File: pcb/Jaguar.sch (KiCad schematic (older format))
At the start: 49 parts, among them P1 12v-SW, P10 TPS, P11 Sensor-GND, P12 O2, P13 Sensor-GND, P14 RPM0+, P15 RPM0-, P16 RPM1+, P17 RPM1-, P20 PT4-7, P22 INJ1-GND, P25 FUEL-, P3 GND, P31 OUT-GND, P32 OUTPUT-12v, P33 Injectors-PB, P34 Injectors-IN, P35 FAN-, P37 ACC-, P39 FAN, P4 BRV-12v, P40 ACC, P41 MAF, P42 INJ2-GND, P43 RPM0-Shield, P44 RPM1-Shield, P45 Sensor-GND, P5 GND2, P50 INJ3-GND, P51 INJ4-GND, P52 INJ8-GND, P53 INJ7-GND, P54 INJ6-GND, P55 INJ5-GND, P56 MAF-CPU-Signal, P6 IAT, P61 Fan-Out, P62 PK5, P7 MAT, P72 INJ1, P73 INJ2, P74 INJ3, P75 INJ4, P76 INJ5, P77 INJ6, P78 INJ7, P79 INJ8, P8 CHT, P9 TPS-5v

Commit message: Rename PK5 to PortK5, Rename FAN-OUT to PortK4, Rename ACC to LSD-2, rename ACC- to LSD2-, Rename FAN to LSD-1, rename FAN- to LSD1-, Rename OUT-GND to OUTPUT-GND.
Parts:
- P35: value FAN- -> LSD1-
- P37: value ACC- -> LSD2-
- P39: value FAN -> LSD-1
- P40: value ACC -> LSD-2
- P61: value Fan-Out -> LSD1-Out
- P62: value PK5 -> PortK5
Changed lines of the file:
@@
-EESchema Schematic File Version 2  date Sun 12 May 2013 06:47:41 PM EDT
+EESchema Schematic File Version 2  date Mon 13 May 2013 11:53:03 AM EDT
 LIBS:opto
 LIBS:power
@@
 Sheet 1 7
 Title "Jaguar PCB for FreeEMS"
-Date "12 may 2013"
+Date "13 may 2013"
 Rev "0.6-alpha"
 Comp "git hash: xxxxxxxxxx"
@@
 P 7050 2100
 F 0 "P62" H 7130 2100 40  0000 L CNN
-F 1 "PK5" H 7050 2155 30  0001 C CNN
+F 1 "PortK5" H 7050 2155 30  0001 C CNN
 	1    7050 2100
 	1    0    0    -1
@@
 P 7500 1900
 F 0 "P61" H 7580 1900 40  0000 L CNN
-F 1 "Fan-Out" H 7500 1955 30  0001 C CNN
+F 1 "LSD1-Out" H 7500 1955 30  0001 C CNN
 	1    7500 1900
 	1    0    0    -1
@@
 P 8350 3000
 F 0 "P39" H 8430 3000 40  0000 L CNN
-F 1 "FAN" H 8350 3055 30  0001 C CNN
+F 1 "LSD-1" H 8350 3055 30  0001 C CNN
 	1    8350 3000
 	-1   0    0    1
@@
 P 8900 3000
 F 0 "P40" H 8980 3000 40  0000 L CNN
-F 1 "ACC" H 8900 3055 30  0001 C CNN
+F 1 "LSD-2" H 8900 3055 30  0001 C CNN
 	1    8900 3000
 	-1   0    0    1
@@
 P 10800 3100
 F 0 "P37" H 10880 3100 40  0000 L CNN
-F 1 "ACC-" H 10800 3155 30  0001 C CNN
+F 1 "LSD2-" H 10800 3155 30  0001 C CNN
 	1    10800 3100
 	1    0    0    -1
@@
 P 10800 3000
 F 0 "P35" H 10880 3000 40  0000 L CNN
-F 1 "FAN-" H 10800 3055 30  0001 C CNN
+F 1 "LSD1-" H 10800 3055 30  0001 C CNN
 	1    10800 3000
 	1    0    0    -1

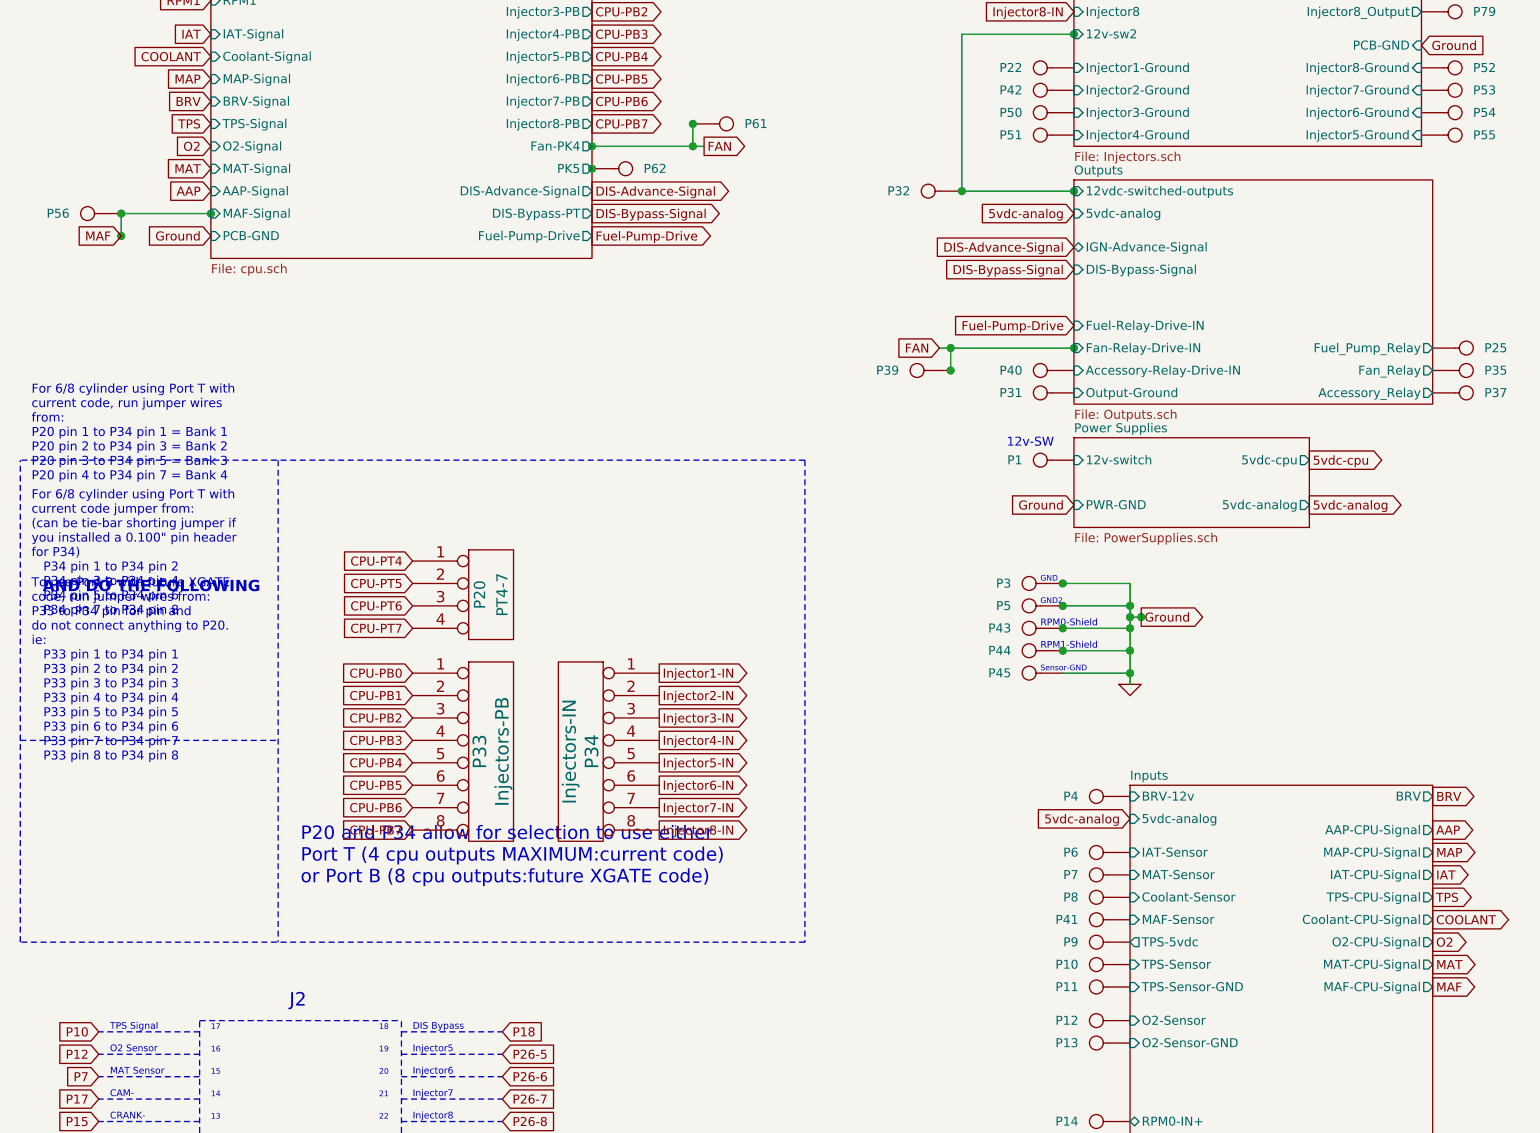
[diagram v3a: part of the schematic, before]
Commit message: Rename MAT to SPR.
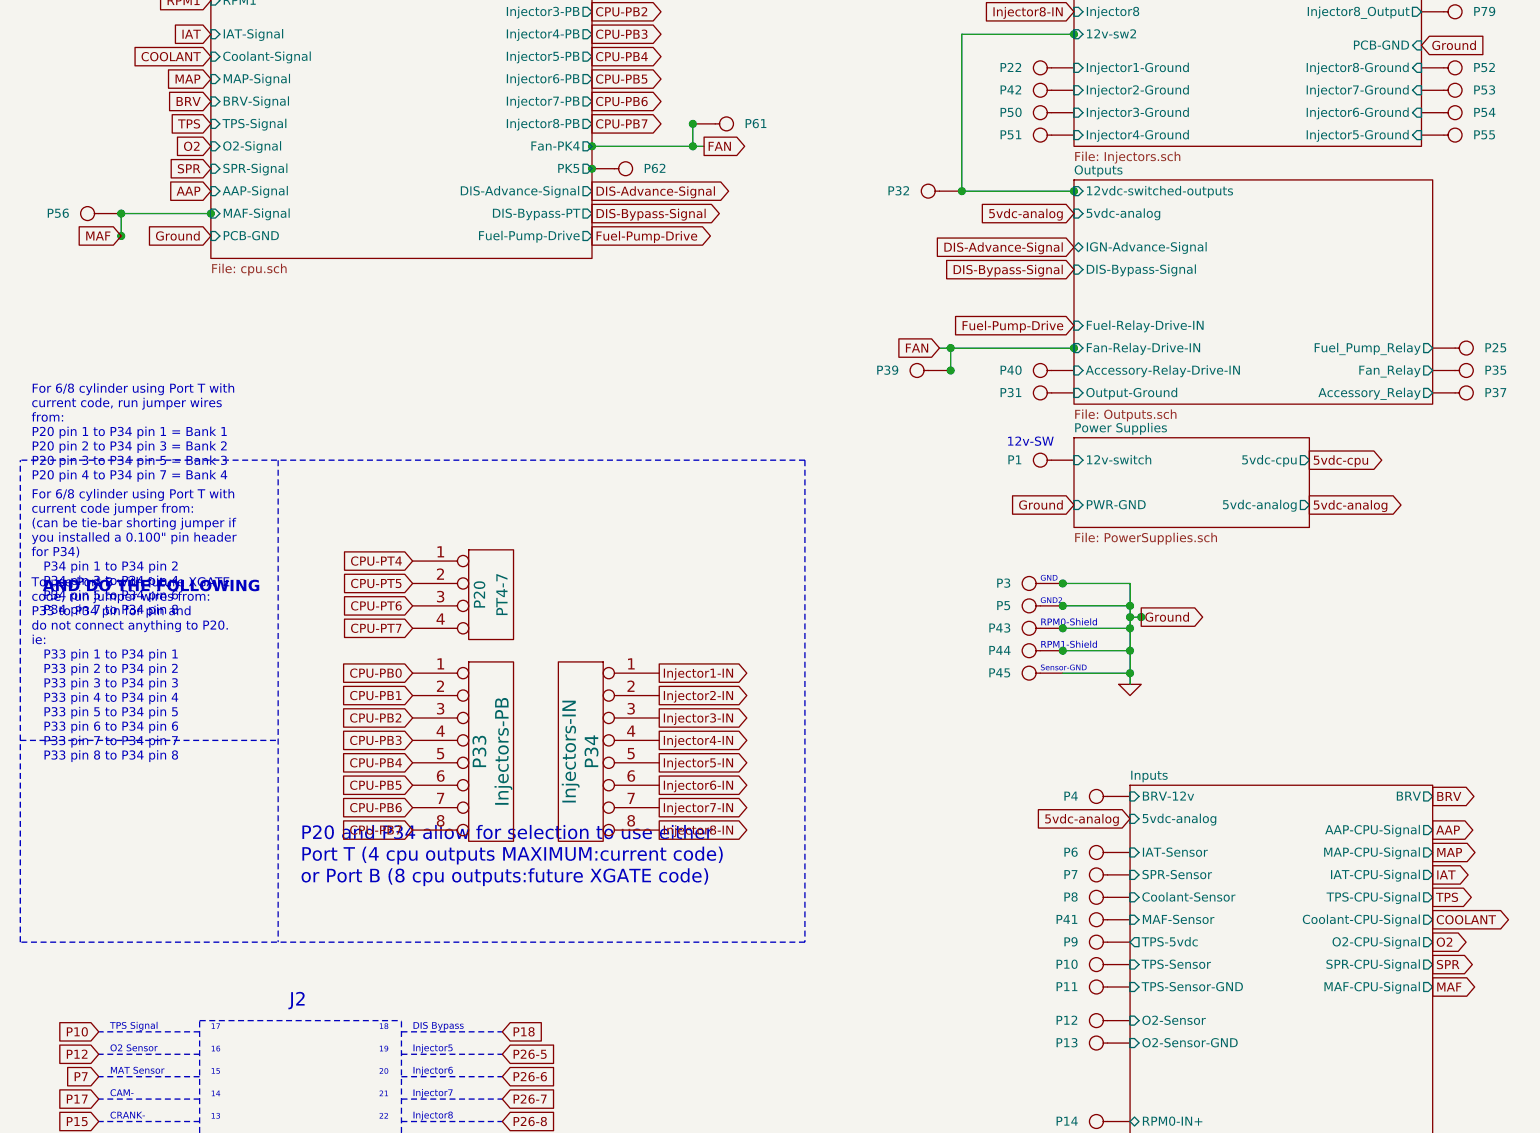
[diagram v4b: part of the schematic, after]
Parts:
- P7: value MAT -> SPR
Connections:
- net Inputs/MAT-Sensor renamed Inputs/SPR-Sensor
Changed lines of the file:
@@
-EESchema Schematic File Version 2  date Mon 13 May 2013 11:53:03 AM EDT
+EESchema Schematic File Version 2  date Mon 13 May 2013 12:23:58 PM EDT
 LIBS:opto
 LIBS:power
@@
 F3 "DIS-Advance-Signal" O R 6900 2200 40
 F4 "MAF-Signal" I L 5200 2300 40
-F5 "MAT-Signal" I L 5200 2100 40
-F6 "BRV-Signal" I L 5200 1800 40
-F7 "MAP-Signal" I L 5200 1700 40
-F8 "O2-Signal" I L 5200 2000 40
-F9 "TPS-Signal" I L 5200 1900 40
-F10 "Coolant-Signal" I L 5200 1600 40
-F11 "IAT-Signal" I L 5200 1500 40
-F12 "AAP-Signal" I L 5200 2200 40
-F13 "5vdc-analog" I L 5200 850 40
-F14 "5vdc-cpu" I L 5200 750 40
-F15 "Injector6-PB" O R 6900 1700 40
-F16 "Injector5-PB" O R 6900 1600 40
-F17 "Injector4-PB" O R 6900 1500 40
-F18 "Injector3-PB" O R 6900 1400 40
-F19 "Injector2-PB" O R 6900 1300 40
-F20 "Injector1-PB" O R 6900 1200 40
-F21 "Injector3-PT" O R 6900 950 40
-F22 "Injector2-PT" O R 6900 850 40
-F23 "Injector1-PT" O R 6900 750 40
-F24 "DIS-Bypass-PT" O R 6900 2300 40
-F25 "Injector4-PT" O R 6900 1050 40
-F26 "Injector8-PB" O R 6900 1900 40
-F27 "Injector7-PB" O R 6900 1800 40
-F28 "PCB-GND" I L 5200 2400 40
-F29 "Fan-PK4" O R 6900 2000 40
-F30 "RPM1" I L 5200 1350 40
-F31 "RPM0" I L 5200 1250 40
-F32 "PK5" O R 6900 2100 40
+F5 "BRV-Signal" I L 5200 1800 40
+F6 "MAP-Signal" I L 5200 1700 40
+F7 "O2-Signal" I L 5200 2000 40
+F8 "TPS-Signal" I L 5200 1900 40
+F9 "Coolant-Signal" I L 5200 1600 40
+F10 "IAT-Signal" I L 5200 1500 40
+F11 "AAP-Signal" I L 5200 2200 40
+F12 "5vdc-analog" I L 5200 850 40
+F13 "5vdc-cpu" I L 5200 750 40
+F14 "Injector6-PB" O R 6900 1700 40
+F15 "Injector5-PB" O R 6900 1600 40
+F16 "Injector4-PB" O R 6900 1500 40
+F17 "Injector3-PB" O R 6900 1400 40
+F18 "Injector2-PB" O R 6900 1300 40
+F19 "Injector1-PB" O R 6900 1200 40
+F20 "Injector3-PT" O R 6900 950 40
+F21 "Injector2-PT" O R 6900 850 40
+F22 "Injector1-PT" O R 6900 750 40
+F23 "DIS-Bypass-PT" O R 6900 2300 40
+F24 "Injector4-PT" O R 6900 1050 40
+F25 "Injector8-PB" O R 6900 1900 40
+F26 "Injector7-PB" O R 6900 1800 40
+F27 "PCB-GND" I L 5200 2400 40
+F28 "Fan-PK4" O R 6900 2000 40
+F29 "RPM1" I L 5200 1350 40
+F30 "RPM0" I L 5200 1250 40
+F31 "PK5" O R 6900 2100 40
+F32 "SPR-Signal" I L 5200 2100 40
 $EndSheet
 Text Notes 650  1200 0    60   ~ 0
@@
 F10 "TPS-CPU-Signal" O R 10650 5350 40
 F11 "TPS-Sensor" I L 9300 5650 40
-F12 "MAT-Sensor" I L 9300 5250 40
-F13 "MAT-CPU-Signal" O R 10650 5650 40
-F14 "BRV" O R 10650 4900 40
-F15 "MAP-CPU-Signal" O R 10650 5150 40
-F16 "BRV-12v" I L 9300 4900 40
-F17 "TPS-5vdc" O L 9300 5550 40
-F18 "5vdc-analog" I L 9300 5000 40
-F19 "MAF-Sensor" I L 9300 5450 40
-F20 "MAF-CPU-Signal" O R 10650 5750 40
-F21 "RPM1-IN-" B L 9300 6650 40
-F22 "RPM0-IN-" B L 9300 6450 40
-F23 "RPM1-IN+" B L 9300 6550 40
-F24 "RPM0-IN+" B L 9300 6350 40
-F25 "RPM1-OUT" B R 10650 6650 40
-F26 "RPM0-OUT" O R 10650 6550 40
-F27 "AAP-CPU-Signal" O R 10650 5050 40
+F12 "BRV" O R 10650 4900 40
+F13 "MAP-CPU-Signal" O R 10650 5150 40
+F14 "BRV-12v" I L 9300 4900 40
+F15 "TPS-5vdc" O L 9300 5550 40
+F16 "5vdc-analog" I L 9300 5000 40
+F17 "MAF-Sensor" I L 9300 5450 40
+F18 "MAF-CPU-Signal" O R 10650 5750 40
+F19 "RPM1-IN-" B L 9300 6650 40
+F20 "RPM0-IN-" B L 9300 6450 40
+F21 "RPM1-IN+" B L 9300 6550 40
+F22 "RPM0-IN+" B L 9300 6350 40
+F23 "RPM1-OUT" B R 10650 6650 40
+F24 "RPM0-OUT" O R 10650 6550 40
+F25 "AAP-CPU-Signal" O R 10650 5050 40
+F26 "SPR-Sensor" I L 9300 5250 40
+F27 "SPR-CPU-Signal" O R 10650 5650 40
 $EndSheet
 Text GLabel 9300 5000 0    40   Input ~ 0
@@
 P 9150 5250
 F 0 "P7" H 9230 5250 40  0000 L CNN
-F 1 "MAT" H 9150 5305 30  0001 C CNN
+F 1 "SPR" H 9150 5305 30  0001 C CNN
 	1    9150 5250
 	-1   0    0    1
@@
 COOLANT
 Text GLabel 5200 2100 0    40   Input ~ 0
-MAT
+SPR
 Text GLabel 10650 5650 2    40   Output ~ 0
-MAT
+SPR
 Text GLabel 5200 1500 0    40   Input ~ 0
 IAT

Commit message: Renamed OUTPUT-12v to IGN-12v as it wasn't clear what this pad was for.
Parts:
- P32: value OUTPUT-12v -> IGN-12v
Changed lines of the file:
@@
-EESchema Schematic File Version 2  date Mon 13 May 2013 12:23:58 PM EDT
+EESchema Schematic File Version 2  date Mon 13 May 2013 10:04:40 PM EDT
 LIBS:opto
 LIBS:power
@@
 Sheet 1 7
 Title "Jaguar PCB for FreeEMS"
-Date "13 may 2013"
+Date "14 may 2013"
 Rev "0.6-alpha"
 Comp "git hash: xxxxxxxxxx"
@@
 P 8400 2200
 F 0 "P32" H 8480 2200 40  0000 L CNN
-F 1 "OUTPUT-12v" H 8400 2255 30  0001 C CNN
+F 1 "IGN-12v" H 8400 2255 30  0001 C CNN
 	1    8400 2200
 	-1   0    0    1

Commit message: Renamed LSD2- to LSD2, renamed LSD-2 to LSD2-IN, renamed FAN- to LSD1, renamed FAN to LSD1-IN, renamed FUEL- to FUEL.
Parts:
- P25: value FUEL- -> FUEL
- P35: value LSD1- -> LSD1
- P37: value LSD2- -> LSD2
- P39: value LSD-1 -> LSD1-IN
- P40: value LSD-2 -> LSD2-IN
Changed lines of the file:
@@
-EESchema Schematic File Version 2  date Mon 13 May 2013 10:04:40 PM EDT
+EESchema Schematic File Version 2  date Tue 14 May 2013 05:29:01 PM EDT
 LIBS:opto
 LIBS:power
@@
 P 8350 3000
 F 0 "P39" H 8430 3000 40  0000 L CNN
-F 1 "LSD-1" H 8350 3055 30  0001 C CNN
+F 1 "LSD1-IN" H 8350 3055 30  0001 C CNN
 	1    8350 3000
 	-1   0    0    1
@@
 P 8900 3000
 F 0 "P40" H 8980 3000 40  0000 L CNN
-F 1 "LSD-2" H 8900 3055 30  0001 C CNN
+F 1 "LSD2-IN" H 8900 3055 30  0001 C CNN
 	1    8900 3000
 	-1   0    0    1
@@
 P 10800 3100
 F 0 "P37" H 10880 3100 40  0000 L CNN
-F 1 "LSD2-" H 10800 3155 30  0001 C CNN
+F 1 "LSD2" H 10800 3155 30  0001 C CNN
 	1    10800 3100
 	1    0    0    -1
@@
 P 10800 3000
 F 0 "P35" H 10880 3000 40  0000 L CNN
-F 1 "LSD1-" H 10800 3055 30  0001 C CNN
+F 1 "LSD1" H 10800 3055 30  0001 C CNN
 	1    10800 3000
 	1    0    0    -1
@@
 P 10800 2900
 F 0 "P25" H 10880 2900 40  0000 L CNN
-F 1 "FUEL-" H 10800 2955 30  0001 C CNN
+F 1 "FUEL" H 10800 2955 30  0001 C CNN
 	1    10800 2900
 	1    0    0    -1

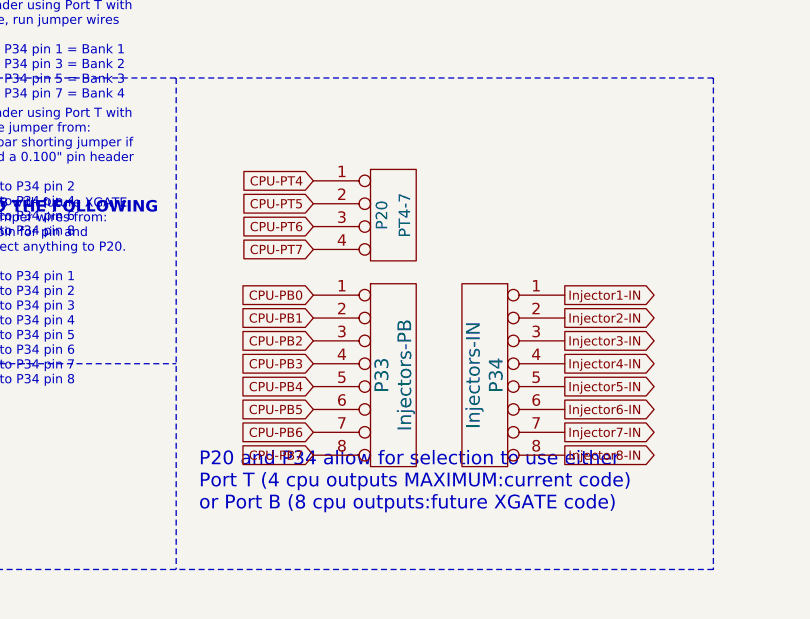
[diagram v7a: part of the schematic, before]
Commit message: Made the CANRX0/CANTX0 into a 0.100" header so that a add-on card could be created later.
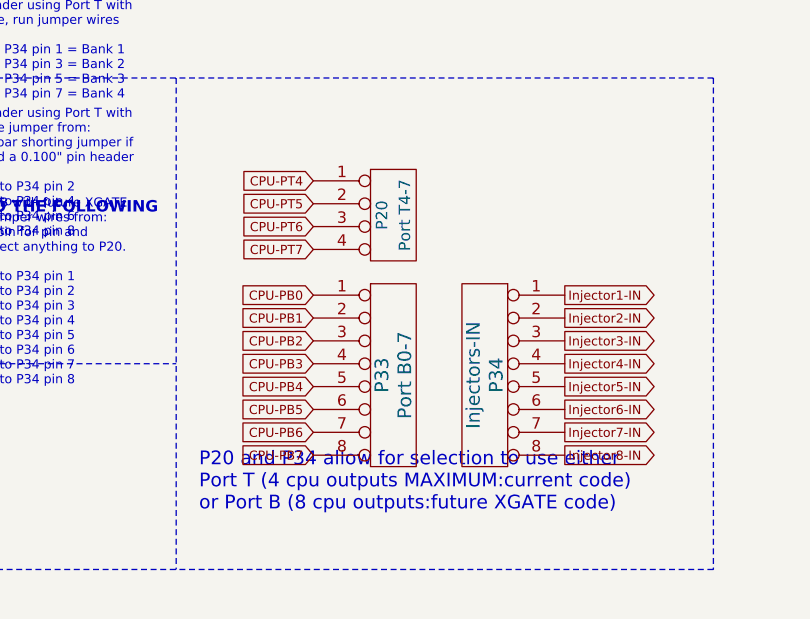
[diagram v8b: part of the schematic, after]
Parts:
- P20: value PT4-7 -> Port T4-7
- P33: value Injectors-PB -> Port B0-7
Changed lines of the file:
@@
-EESchema Schematic File Version 2  date Wed 15 May 2013 02:06:49 PM EDT
+EESchema Schematic File Version 2  date Tue 21 May 2013 04:54:21 PM EDT
 LIBS:opto
 LIBS:power
@@
 Sheet 1 7
 Title "Jaguar PCB for FreeEMS"
-Date "15 may 2013"
+Date "21 may 2013"
 Rev "0.6-alpha"
 Comp "git hash: xxxxxxxxxx"
@@
 P 6450 4000
 F 0 "P20" V 6400 4000 50  0000 C CNN
-F 1 "PT4-7" V 6500 4000 50  0000 C CNN
+F 1 "Port T4-7" V 6500 4000 50  0000 C CNN
 	1    6450 4000
 	1    0    0    -1
@@
 P 6450 4700
 F 0 "P33" V 6400 4700 60  0000 C CNN
-F 1 "Injectors-PB" V 6500 4700 60  0000 C CNN
+F 1 "Port B0-7" V 6500 4700 60  0000 C CNN
 	1    6450 4700
 	1    0    0    -1
